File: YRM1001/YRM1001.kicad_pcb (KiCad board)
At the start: 2 copper layers, 35 x 35 mm, 15 parts, among them J1 picoblade, J2 Conn_01x05

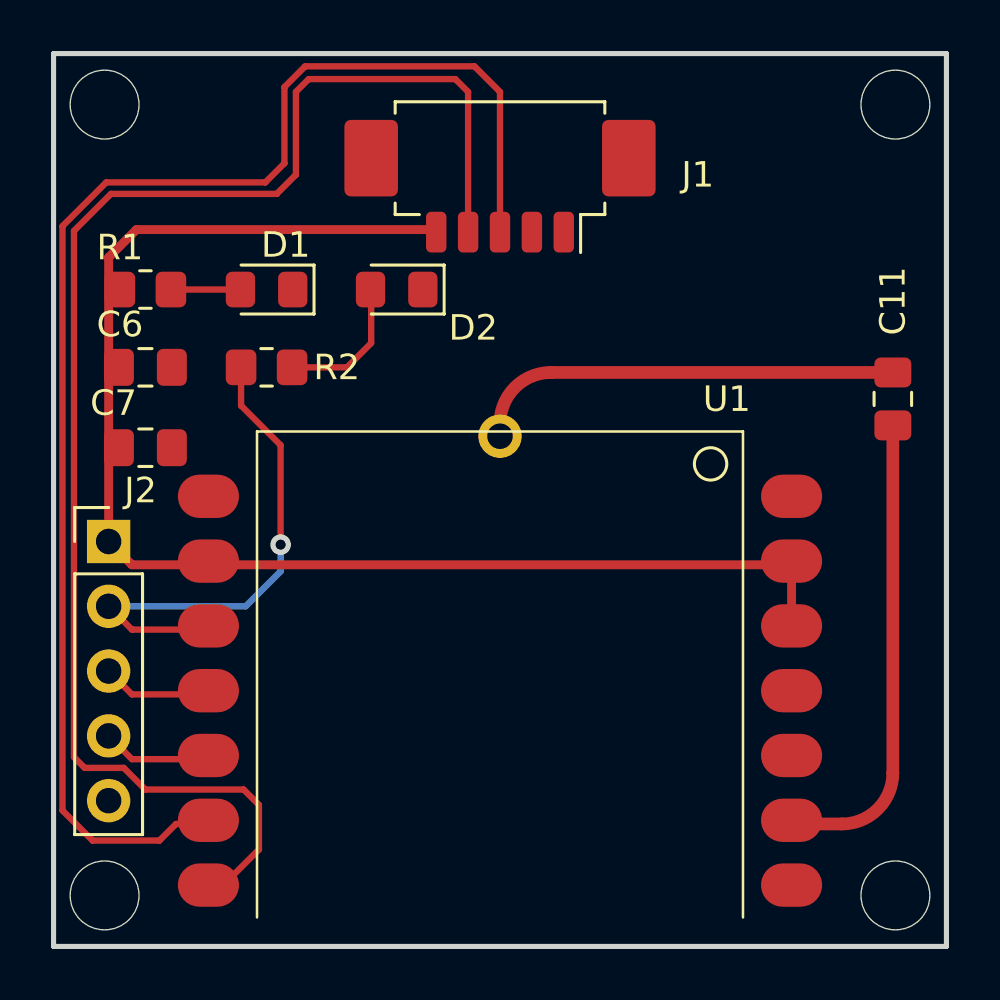
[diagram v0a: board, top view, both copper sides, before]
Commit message: Add files via upload
updated board version to 1.2:
- changed ICSP from 10 pin header to 6 pin header. 10 pin ICSP connections can be done with a 6 to 10 pin adapter cable.
- changed name on board to UHF | RFID | SAM, removing '1/2 nard' from the name for clarity on what the board is and does.
- removed header that was meant to hard-connect the UHF module to the board: it is not used for communication with the board after all. 
- updated the QR codes designs for better machine readability
- various routing improvements.

schematics:
- changed ICSP from 10 pin header to 6 pin header

other:
reverse-engineered the YRM1001 and YRM200 boards to have them in Kicad. Measurements should be close enough for OKing designs using those modules.
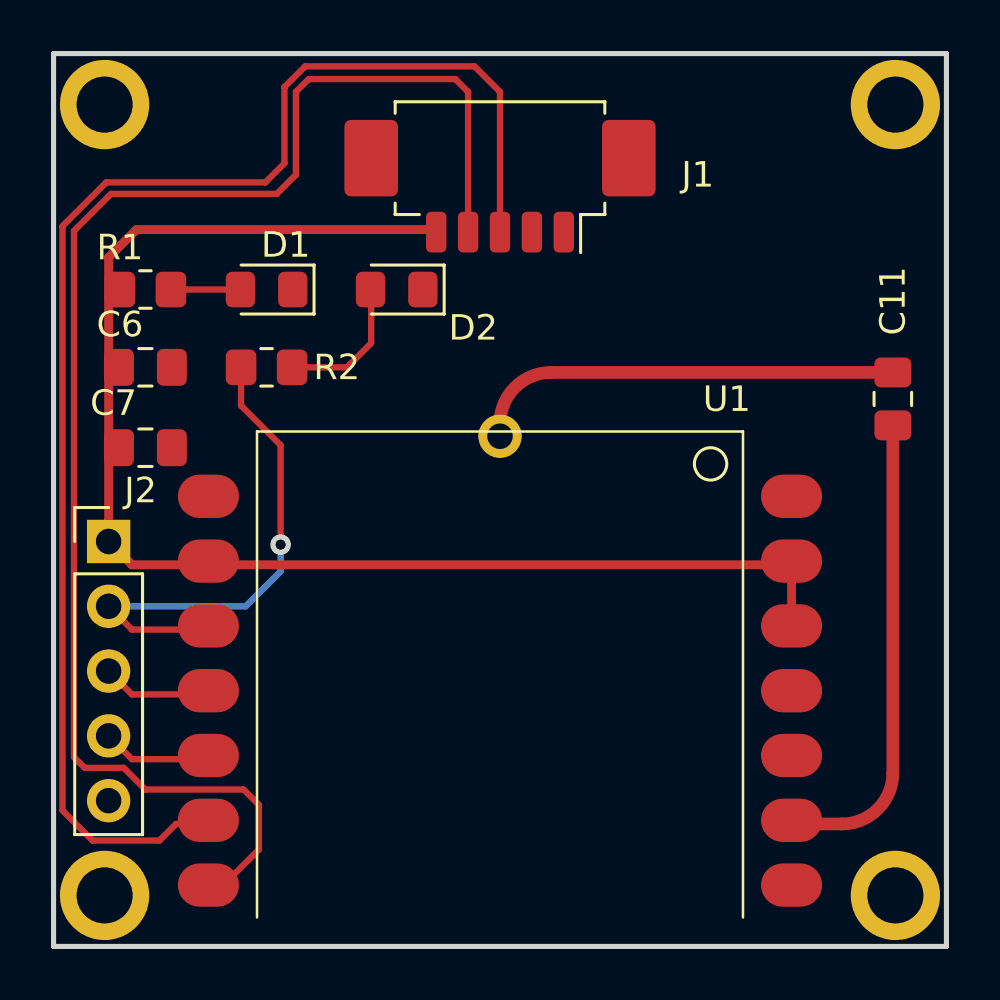
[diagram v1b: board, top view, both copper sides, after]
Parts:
- AE1: value Antenna_Chip -> Antenna
- H1, H2, H3, H4: renamed from ?; value (none) -> MountingHole_Pad; footprint (none) -> MountingHole:MountingHole_2.2mm_M2_ISO7380_Pad
